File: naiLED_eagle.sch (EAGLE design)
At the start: 8 parts, among them IC1 TCS3414, U2 24LC00T-I/OT, U3 ATTINY25-20SSU

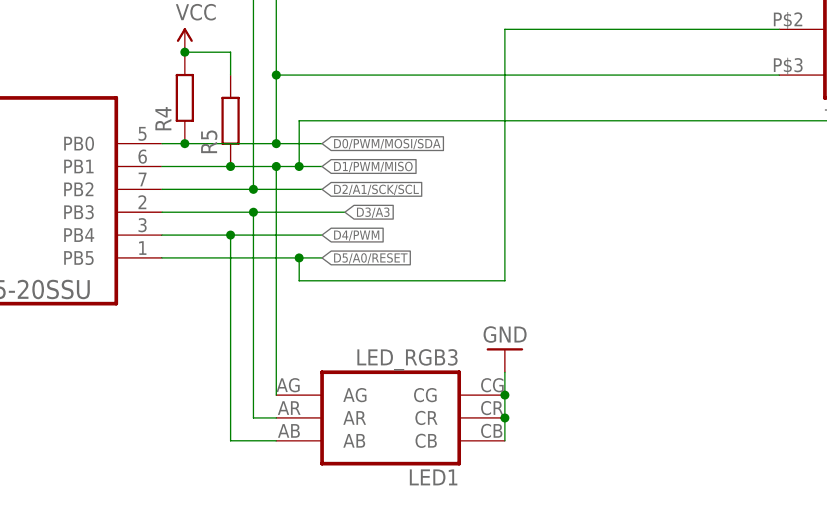
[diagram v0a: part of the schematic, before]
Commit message: miniSK led
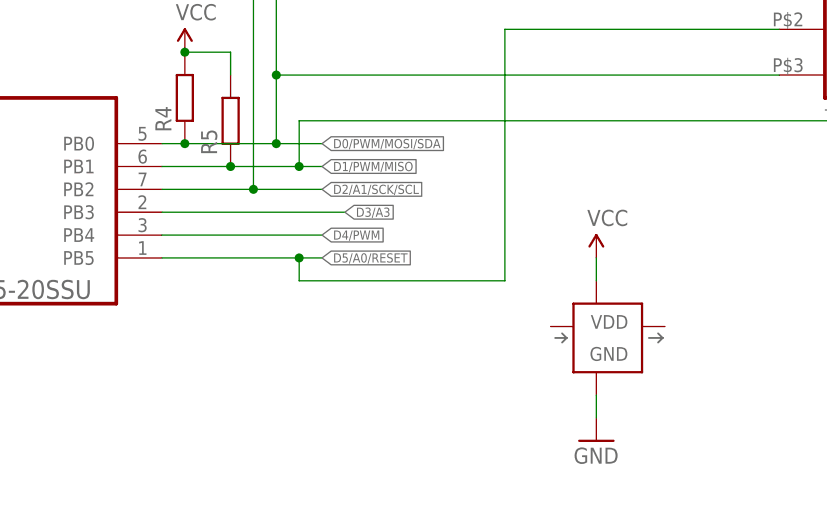
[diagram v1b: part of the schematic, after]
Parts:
- removed LED1: LED_RGB3, dp_devices:LED_RGB3
- added U$1: SK6812MINI, pimoroni-optoelectronics:SK6812MINI
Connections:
- net D1/PWM/MISO: no longer LED1.AG
- net D3/A3: no longer LED1.AR
- net D4/PWM: no longer LED1.AB
- net GND: now also U$1.GND; no longer LED1.CB, LED1.CG, LED1.CR
- net VCC: now also U$1.VDD

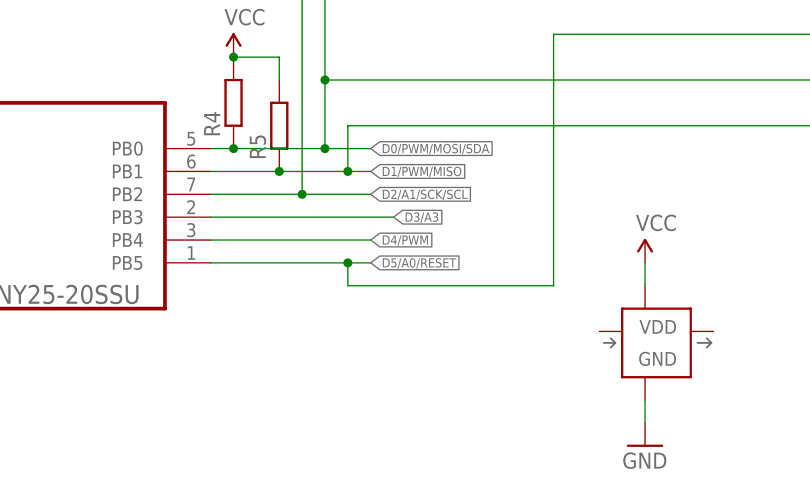
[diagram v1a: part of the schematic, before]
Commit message: changed attiny25 footprint to 85, ripup
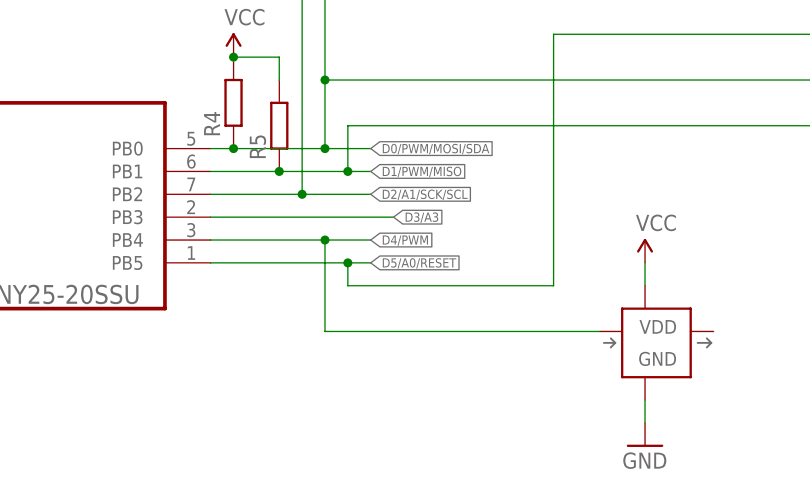
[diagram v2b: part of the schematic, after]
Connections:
- net D4/PWM: now also U$1.DI
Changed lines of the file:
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@@
 <pinref part="U3" gate="A" pin="PB4"/>
 <label x="35.56" y="20.32" size="1.016" layer="95" xref="yes"/>
-<wire x1="17.78" y1="20.32" x2="35.56" y2="20.32" width="0.1524" layer="91"/>
+<wire x1="17.78" y1="20.32" x2="30.48" y2="20.32" width="0.1524" layer="91"/>
+<wire x1="30.48" y1="20.32" x2="35.56" y2="20.32" width="0.1524" layer="91"/>
+<wire x1="30.48" y1="20.32" x2="30.48" y2="10.16" width="0.1524" layer="91"/>
+<junction x="30.48" y="20.32"/>
+<pinref part="U$1" gate="G$1" pin="DI"/>
+<wire x1="30.48" y1="10.16" x2="60.96" y2="10.16" width="0.1524" layer="91"/>
 </segment>
 </net>

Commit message: routing mid
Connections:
- removed net D5/A0/RESET: IC1.SYNC, U3.PB5
- net D3/A3: now also IC1.SYNC
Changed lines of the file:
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@@
 <grid distance="0.1" unitdist="inch" unit="inch" style="lines" multiple="1" display="no" altdistance="0.01" altunitdist="inch" altunit="inch"/>
 <layers>
-<layer number="1" name="Top" color="4" fill="1" visible="yes" active="no"/>
+<layer number="1" name="Top" color="4" fill="1" visible="no" active="no"/>
 <layer number="2" name="Route2" color="1" fill="3" visible="no" active="no"/>
 <layer number="3" name="Route3" color="4" fill="3" visible="no" active="no"/>
@@
 <layer number="14" name="Route14" color="1" fill="6" visible="no" active="no"/>
 <layer number="15" name="Route15" color="4" fill="6" visible="no" active="no"/>
-<layer number="16" name="Bottom" color="1" fill="1" visible="yes" active="no"/>
-<layer number="17" name="Pads" color="2" fill="1" visible="yes" active="no"/>
-<layer number="18" name="Vias" color="2" fill="1" visible="yes" active="no"/>
-<layer number="19" name="Unrouted" color="6" fill="1" visible="yes" active="no"/>
-<layer number="20" name="Dimension" color="15" fill="1" visible="yes" active="no"/>
-<layer number="21" name="tPlace" color="7" fill="1" visible="yes" active="no"/>
-<layer number="22" name="bPlace" color="7" fill="1" visible="yes" active="no"/>
-<layer number="23" name="tOrigins" color="15" fill="1" visible="yes" active="no"/>
-<layer number="24" name="bOrigins" color="15" fill="1" visible="yes" active="no"/>
-<layer number="25" name="tNames" color="7" fill="1" visible="yes" active="no"/>
-<layer number="26" name="bNames" color="7" fill="1" visible="yes" active="no"/>
-<layer number="27" name="tValues" color="7" fill="1" visible="yes" active="no"/>
-<layer number="28" name="bValues" color="7" fill="1" visible="yes" active="no"/>
+<layer number="16" name="Bottom" color="1" fill="1" visible="no" active="no"/>
+<layer number="17" name="Pads" color="2" fill="1" visible="no" active="no"/>
+<layer number="18" name="Vias" color="2" fill="1" visible="no" active="no"/>
+<layer number="19" name="Unrouted" color="6" fill="1" visible="no" active="no"/>
+<layer number="20" name="Dimension" color="15" fill="1" visible="no" active="no"/>
+<layer number="21" name="tPlace" color="7" fill="1" visible="no" active="no"/>
+<layer number="22" name="bPlace" color="7" fill="1" visible="no" active="no"/>
+<layer number="23" name="tOrigins" color="15" fill="1" visible="no" active="no"/>
+<layer number="24" name="bOrigins" color="15" fill="1" visible="no" active="no"/>
+<layer number="25" name="tNames" color="7" fill="1" visible="no" active="no"/>
+<layer number="26" name="bNames" color="7" fill="1" visible="no" active="no"/>
+<layer number="27" name="tValues" color="7" fill="1" visible="no" active="no"/>
+<layer number="28" name="bValues" color="7" fill="1" visible="no" active="no"/>
 <layer number="29" name="tStop" color="7" fill="3" visible="no" active="no"/>
 <layer number="30" name="bStop" color="7" fill="6" visible="no" active="no"/>
@@
 <layer number="35" name="tGlue" color="7" fill="4" visible="no" active="no"/>
 <layer number="36" name="bGlue" color="7" fill="5" visible="no" active="no"/>
-<layer number="37" name="tTest" color="7" fill="1" visible="yes" active="no"/>
-<layer number="38" name="bTest" color="7" fill="1" visible="yes" active="no"/>
+<layer number="37" name="tTest" color="7" fill="1" visible="no" active="no"/>
+<layer number="38" name="bTest" color="7" fill="1" visible="no" active="no"/>
 <layer number="39" name="tKeepout" color="4" fill="11" visible="no" active="no"/>
 <layer number="40" name="bKeepout" color="1" fill="11" visible="no" active="no"/>
@@
 <layer number="44" name="Drills" color="7" fill="1" visible="no" active="no"/>
 <layer number="45" name="Holes" color="7" fill="1" visible="no" active="no"/>
-<layer number="46" name="Milling" color="3" fill="1" visible="yes" active="no"/>
-<layer number="47" name="Measures" color="7" fill="1" visible="yes" active="no"/>
-<layer number="48" name="Document" color="7" fill="1" visible="yes" active="no"/>
-<layer number="49" name="Reference" color="7" fill="1" visible="yes" active="no"/>
-<layer number="50" name="dxf" color="7" fill="1" visible="yes" active="no"/>
-<layer number="51" name="tDocu" color="7" fill="1" visible="yes" active="no"/>
-<layer number="52" name="bDocu" color="7" fill="1" visible="yes" active="no"/>
-<layer number="53" name="tGND_GNDA" color="7" fill="1" visible="yes" active="no"/>
-<layer number="54" name="bGND_GNDA" color="7" fill="1" visible="yes" active="no"/>
-<layer number="56" name="wert" color="7" fill="1" visible="yes" active="no"/>
+<layer number="46" name="Milling" color="3" fill="1" visible="no" active="no"/>
+<layer number="47" name="Measures" color="7" fill="1" visible="no" active="no"/>
+<layer number="48" name="Document" color="7" fill="1" visible="no" active="no"/>
+<layer number="49" name="Reference" color="7" fill="1" visible="no" active="no"/>
+<layer number="50" name="dxf" color="7" fill="1" visible="no" active="no"/>
+<layer number="51" name="tDocu" color="7" fill="1" visible="no" active="no"/>
+<layer number="52" name="bDocu" color="7" fill="1" visible="no" active="no"/>
+<layer number="53" name="tGND_GNDA" color="7" fill="1" visible="no" active="no"/>
+<layer number="54" name="bGND_GNDA" color="7" fill="1" visible="no" active="no"/>
+<layer number="56" name="wert" color="7" fill="1" visible="no" active="no"/>
 <layer number="57" name="tCAD" color="7" fill="1" visible="no" active="no"/>
 <layer number="91" name="Nets" color="2" fill="1" visible="yes" active="yes"/>
@@
 <segment>
 <pinref part="U3" gate="A" pin="PB2"/>
-<label x="35.56" y="25.4" size="1.016" layer="95" xref="yes"/>
-<wire x1="35.56" y1="25.4" x2="27.94" y2="25.4" width="0.1524" layer="91"/>
+<label x="38.1" y="25.4" size="1.016" layer="95" xref="yes"/>
+<wire x1="38.1" y1="25.4" x2="27.94" y2="25.4" width="0.1524" layer="91"/>
 <pinref part="IC1" gate="A" pin="SCL"/>
 <wire x1="27.94" y1="25.4" x2="17.78" y2="25.4" width="0.1524" layer="91"/>
@@
 </segment>
 </net>
-<net name="D5/A0/RESET" class="0">
-<segment>
-<pinref part="U3" gate="A" pin="PB5"/>
-<label x="35.56" y="17.78" size="1.016" layer="95" xref="yes"/>
-<wire x1="35.56" y1="17.78" x2="33.02" y2="17.78" width="0.1524" layer="91"/>
-<pinref part="IC1" gate="A" pin="SYNC"/>
-<wire x1="33.02" y1="17.78" x2="17.78" y2="17.78" width="0.1524" layer="91"/>
-<wire x1="86.36" y1="43.18" x2="55.88" y2="43.18" width="0.1524" layer="91"/>
-<wire x1="55.88" y1="43.18" x2="55.88" y2="15.24" width="0.1524" layer="91"/>
-<wire x1="55.88" y1="15.24" x2="33.02" y2="15.24" width="0.1524" layer="91"/>
-<wire x1="33.02" y1="15.24" x2="33.02" y2="17.78" width="0.1524" layer="91"/>
-<junction x="33.02" y="17.78"/>
-</segment>
-</net>
 <net name="VCC" class="0">
 <segment>
@@
 <segment>
 <pinref part="U3" gate="A" pin="PB4"/>
-<label x="35.56" y="20.32" size="1.016" layer="95" xref="yes"/>
+<label x="38.1" y="20.32" size="1.016" layer="95" xref="yes"/>
 <wire x1="17.78" y1="20.32" x2="30.48" y2="20.32" width="0.1524" layer="91"/>
-<wire x1="30.48" y1="20.32" x2="35.56" y2="20.32" width="0.1524" layer="91"/>
+<wire x1="30.48" y1="20.32" x2="38.1" y2="20.32" width="0.1524" layer="91"/>
 <wire x1="30.48" y1="20.32" x2="30.48" y2="10.16" width="0.1524" layer="91"/>
 <junction x="30.48" y="20.32"/>
@@
 </segment>
 </net>
-<net name="D3/A3" class="0">
-<segment>
-<pinref part="U3" gate="A" pin="PB3"/>
-<label x="38.1" y="22.86" size="1.016" layer="95" xref="yes"/>
-<wire x1="17.78" y1="22.86" x2="38.1" y2="22.86" width="0.1524" layer="91"/>
-</segment>
-</net>
 <net name="D1/PWM/MISO" class="0">
 <segment>
 <pinref part="U3" gate="A" pin="PB1"/>
 <wire x1="17.78" y1="27.94" x2="25.4" y2="27.94" width="0.1524" layer="91"/>
-<label x="35.56" y="27.94" size="1.016" layer="95" xref="yes"/>
+<label x="38.1" y="27.94" size="1.016" layer="95" xref="yes"/>
 <wire x1="25.4" y1="27.94" x2="33.02" y2="27.94" width="0.1524" layer="91"/>
-<wire x1="33.02" y1="27.94" x2="35.56" y2="27.94" width="0.1524" layer="91"/>
+<wire x1="33.02" y1="27.94" x2="38.1" y2="27.94" width="0.1524" layer="91"/>
 <pinref part="R5" gate="G$1" pin="1"/>
 <junction x="25.4" y="27.94"/>
@@
 <pinref part="U3" gate="A" pin="PB0"/>
 <wire x1="20.32" y1="30.48" x2="30.48" y2="30.48" width="0.1524" layer="91"/>
-<label x="35.56" y="30.48" size="1.016" layer="95" xref="yes"/>
+<label x="38.1" y="30.48" size="1.016" layer="95" xref="yes"/>
 <pinref part="IC1" gate="A" pin="SDA"/>
-<wire x1="30.48" y1="30.48" x2="35.56" y2="30.48" width="0.1524" layer="91"/>
+<wire x1="30.48" y1="30.48" x2="38.1" y2="30.48" width="0.1524" layer="91"/>
 <wire x1="86.36" y1="38.1" x2="30.48" y2="38.1" width="0.1524" layer="91"/>
 <wire x1="30.48" y1="38.1" x2="30.48" y2="30.48" width="0.1524" layer="91"/>
@@
 </segment>
 </net>
+<net name="D3/A3" class="0">
+<segment>
+<pinref part="IC1" gate="A" pin="SYNC"/>
+<wire x1="86.36" y1="43.18" x2="35.56" y2="43.18" width="0.1524" layer="91"/>
+<pinref part="U3" gate="A" pin="PB3"/>
+<label x="38.1" y="22.86" size="1.016" layer="95" xref="yes"/>
+<wire x1="17.78" y1="22.86" x2="35.56" y2="22.86" width="0.1524" layer="91"/>
+<wire x1="35.56" y1="22.86" x2="38.1" y2="22.86" width="0.1524" layer="91"/>
+<wire x1="35.56" y1="43.18" x2="35.56" y2="22.86" width="0.1524" layer="91"/>
+<junction x="35.56" y="22.86"/>
+</segment>
+</net>
